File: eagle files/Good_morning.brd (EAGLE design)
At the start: 37 x 67 mm, 67 parts, among them J2 20329, Q1 mmbt2222, Q2 mmbt2222, SW1 K2-1817UQ-C4SW-01, SW2 KMR2, U1 DRV8825PWP, U2 AP2112-3.3, U3 VEML6030, U4 ESP32_WROOM32_SKINNY, U5 CP2104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

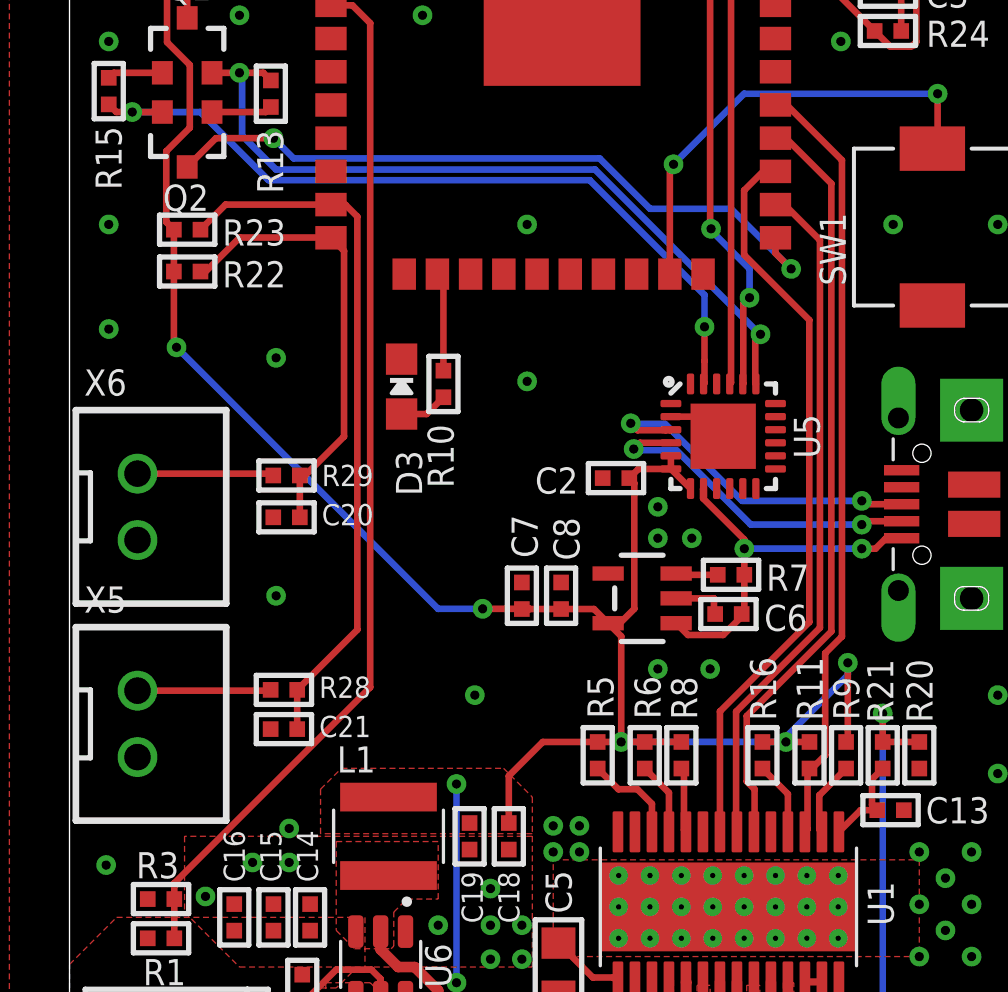
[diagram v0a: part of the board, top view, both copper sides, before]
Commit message: fixes mentioned in readme errata
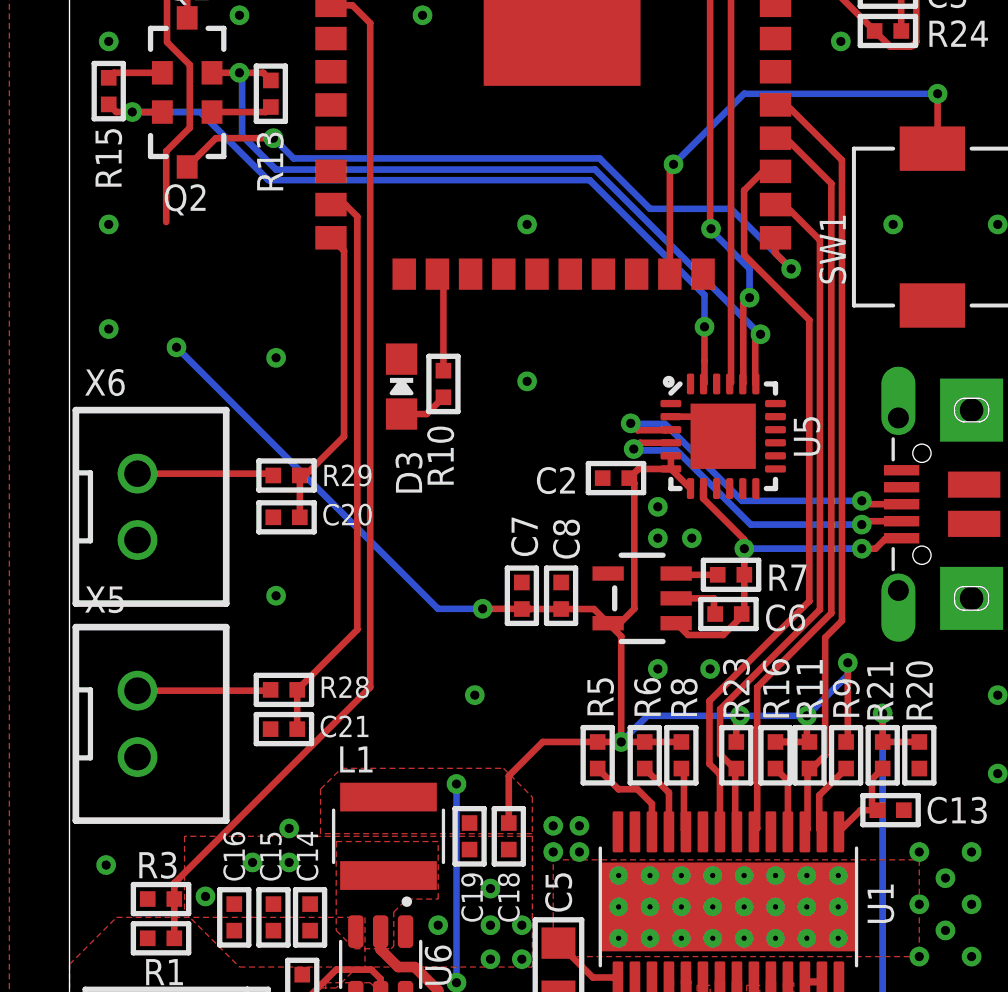
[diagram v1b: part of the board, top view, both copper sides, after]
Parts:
- removed R22: 10k, microbuilder:_0402
- moved R23 29.1 mm to (7.00, -10.3), turned to 270 degrees
- moved R16 0.50 mm to (8.50, -10.3)
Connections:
- net 3.3V: no longer R22.1
- net ENA: now also R23.2
- net LIM_1: no longer R23.2
- net LIM_2: no longer R22.2
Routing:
- net LIM_2: track 17.4 -> 11.8 mm
- net LIM_1: track 27.1 -> 21.8 mm
- net 3.3V: track 136.3 -> 133.6 mm, vias 9 -> 10
- net ENA: track 26.2 -> 26.8 mm
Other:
- board text added: "Curtain Controller v2 25/01/2020"
- board text removed: "Curtain Controller v1 09/01/2020"
